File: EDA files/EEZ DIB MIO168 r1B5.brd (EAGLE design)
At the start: 146 x 95 mm, 301 parts, among them IC1 M24C32-WMN6P, IC10 DAC7760IPWPR, IC11 DAC7760IPWPR, IC12 OPA376AIDBVR, IC13 DAC7563TDGSR, IC14 OPA2196IDR, IC15 BTS3408G, IC16 BTS3408G, IC17 BTS3408G, IC18 BTS3408G, IC19 74HC126PW,118, IC2 Si8641BB-B-IS1, IC20 TL431B, IC21 DG468DV-T1-E3, IC22 DG468DV-T1-E3, IC23 DG468DV-T1-E3, IC24 DG468DV-T1-E3, IC25 DG468DV-T1-E3, IC26 DG468DV-T1-E3, IC27 DG468DV-T1-E3, IC28 DG468DV-T1-E3, IC29 DG468DV-T1-E3, IC3 Si8641BB-B-IS1, IC30 DG468DV-T1-E3, IC31 DG468DV-T1-E3, IC32 DG468DV-T1-E3, IC33 DG468DV-T1-E3, IC34 DG468DV-T1-E3, IC35 OPA376AIDBVR, IC36 ADS8674IDBT, IC4 L78L12, IC5 LM1117MP-5.0, IC6 LP2985-33DBVR, IC7 L79L12, IC8 STM32F446ZCT6, IC9 OPA2196IDR, J1 4907, J2 N.C., Q1 2N7002PS,115, Q10 BSS169, Q11 BSS169, Q12 BSS169, Q13 BSS169, Q2 2N7002PS,115, Q3 2N7002PS,115, Q4 2N7002PS,115, Q5 2N7002PS,115, Q6 BSS169, Q7 BSS169, Q8 BSS169, Q9 BSS169, X1 77317-104-28LF, X2 SSW-106-02-S-S, X3 691327310016, X4 691327310016, X5 1-2314878-0, X6 1-2314878-0, X7 1-2314878-0, Y1 25MHz

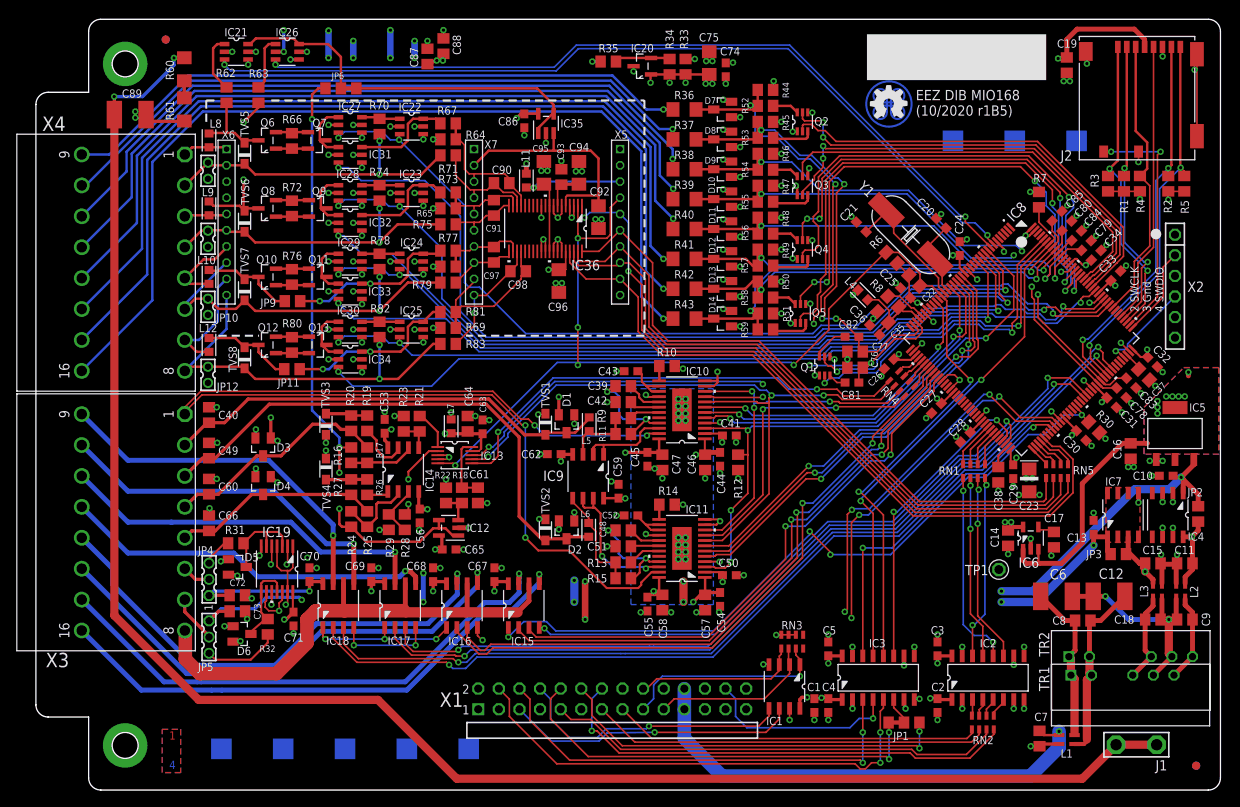
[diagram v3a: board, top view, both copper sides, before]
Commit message: ZD1, ZD2 added
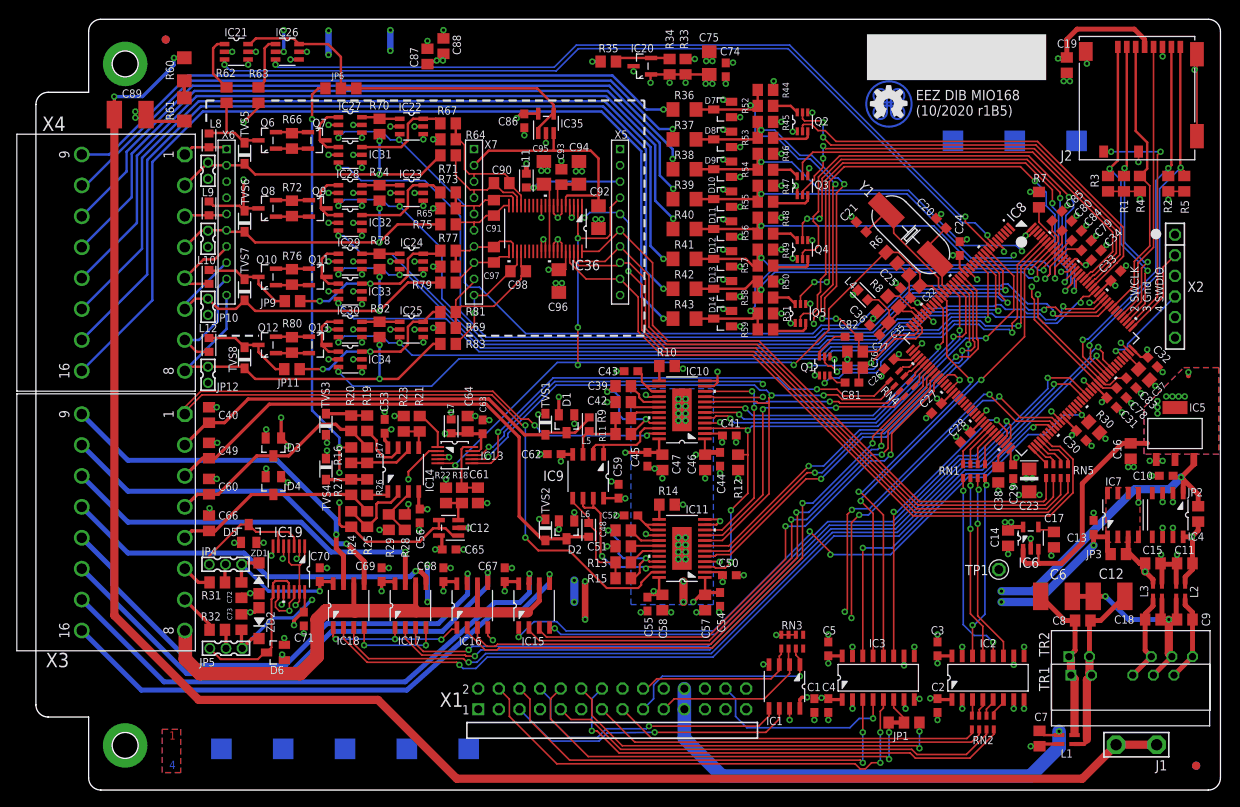
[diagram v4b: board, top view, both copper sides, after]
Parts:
- removed SH4: (no value), EEZ_Lib1:SHORT_NOHOLE
- added SH1: (no value), EEZ_Lib1:SHORT_NOHOLE
- added ZD1, ZD2: MMSZ4700T1G, EEZ_Lib1:SOD123
- moved SH2 26.8 mm to (18.2, 19.7), turned to 270 degrees
- moved R32 6.23 mm to (22.4, 19.7), turned to 180 degrees
- moved R31 5.34 mm to (22.4, 25.6), turned to 180 degrees
- moved D6 4.72 mm to (29.5, 17.0), turned to 90 degrees
- moved D5 4.36 mm to (26.2, 31.6), turned to 0 degrees
- moved JP4 2.74 mm to (23.4, 27.8), turned to 180 degrees
- moved JP5 2.52 mm to (23.4, 17.5), turned to 180 degrees
- moved IC19 1.46 mm to (31.2, 27.2)
- moved C73 1.43 mm to (25.3, 20.7), turned to 90 degrees
- moved C70 1.27 mm to (35.0, 26.5)
- moved C71 1.27 mm to (33.0, 21.1)
- moved IC16 1.27 mm to (53.8, 22.7)
- moved D3 1.27 mm to (29.3, 42.3)
- moved D4 1.27 mm to (29.3, 37.5)
- moved C67 1.27 mm to (57.8, 26.5)
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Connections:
- net +12V_ISO: now also ZD1.C
- net +3V3_ISO: now also D5.2, D6.2
- net +5V_ISO: no longer D5.2, D6.2
- net -12V_ISO: now also ZD2.C
- net -VSENSE: now also SH1.2; no longer SH2.2
- net GND: now also SH1.1, ZD1.A, ZD2.A; no longer SH4.1
- net N$1: now also SH2.2; no longer SH4.2
- net N$129: now also JP4.1; no longer R31.2
- net N$134: now also JP5.1; no longer R32.2
- net N$22: now also JP4.2; no longer JP4.1
- net N$25: now also R31.2; no longer JP4.2
- net N$39: now also R32.2; no longer JP5.2
- net N$40: now also JP5.2; no longer JP5.1
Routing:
- net +5V_ISO: track 282.3 -> 177.0 mm, vias 11 -> 9
- net N$134: track 11.0 -> 20.1 mm
- net N$40: track 9.45 -> 3.19 mm
- net -12V_ISO: track 260.8 -> 257.0 mm
- net N$129: track 12.3 -> 15.5 mm
- net +3V3_ISO: track 103.3 -> 106.4 mm, vias 35 -> 37
- net GND: track 228.3 -> 230.6 mm
- net +12V_ISO: track 262.5 -> 260.2 mm, vias 15 -> 14
- net N$1: track 73.5 -> 75.7 mm
- net OUT_EN: track 132.2 -> 130.1 mm
- net PWM#1: track 126.5 -> 124.4 mm
- net DOUT4: track 79.7 -> 78.0 mm
- net DOUT5: track 78.6 -> 76.9 mm
- net N$22: track 3.68 -> 2.25 mm
- net POUT5: track 61.6 -> 62.9 mm
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
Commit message: PWM outputs pin rearrangement
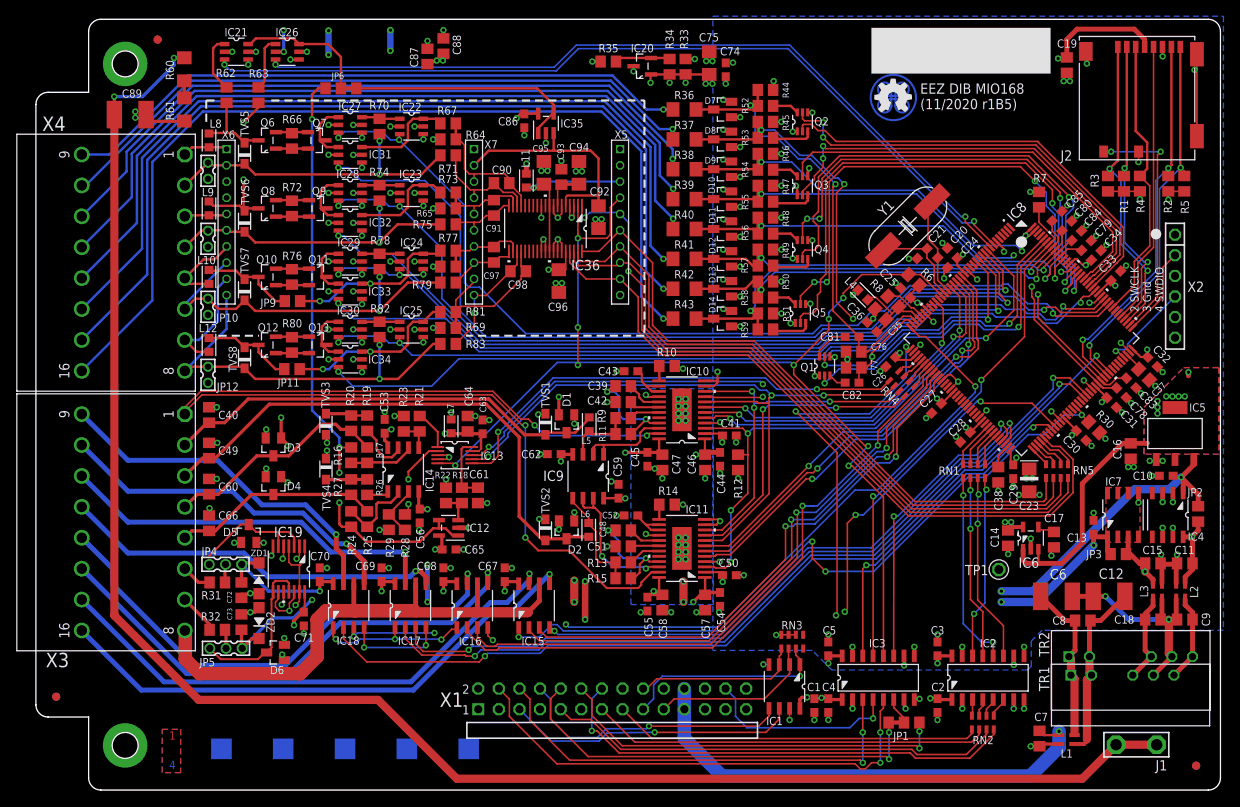
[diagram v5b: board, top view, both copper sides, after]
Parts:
- removed C22: N.C., rcl:C0805
- added FM3: FIDUCIAL_2, EEZ_Lib1:FIDUCIAL_DUAL
- R60, R61: value 560K -> 470K
- moved C21 8.18 mm to (109.2, 66.1), turned to 45 degrees
- moved C82 5.66 mm to (100.6, 50.2)
- moved C81 5.64 mm to (100.6, 55.9)
- moved R6 3.86 mm to (108.2, 62.9)
- moved C20 3.65 mm to (111.7, 66.2), turned to 225 degrees
- moved C77 1.98 mm to (100.8, 52.1)
- moved C24 1.97 mm to (113.0, 65.0), turned to 225 degrees
- moved C76 1.96 mm to (100.8, 54.0)
- moved Y1 1.13 mm to (107.5, 69.5), turned to 45 degrees
- moved FM1 1.00 mm to (15.0, 92.5)
- moved EEZ_SIGNATURE 0.97 mm to (105.7, 85.4)
- moved C36 0.49 mm to (103.0, 57.1)
- moved C35 0.46 mm to (104.1, 58.6)
- moved C26 0.34 mm to (105.4, 52.8)
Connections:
- net N$52 renamed +12V_CM
- net N$53 renamed GND_CM
- net !RESET: no longer C22.1
- net +3V3_ISO: no longer C22.2
- net DOUT1: now also IC8.36; no longer IC8.101
- net N$24: now also Q1.6; no longer Q1.3
- net N$76: now also Q1.3; no longer Q1.6
- net PWM#2: now also IC8.37; no longer IC8.82
- net SLOW_DIN#0: now also Q1.2; no longer Q1.5
- net SLOW_DIN#1: now also Q1.5; no longer Q1.2
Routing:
- net !RESET: track 160.6 -> 147.1 mm, vias 7 -> 9
- net DIN0: track 71.0 -> 58.0 mm, vias 5 -> 2
- net DOUT1: track 114.5 -> 102.2 mm, vias 2 -> 4
- net RCC_OSC_OUT: track 16.5 -> 11.8 mm
- net +3V3_ISO: track 106.4 -> 103.5 mm
- net RCC_OSC_IN: track 9.38 -> 12.1 mm
- net N$24: track 2.22 -> 4.63 mm
- net SLOW_DIN#1: track 41.1 -> 38.7 mm
- net N$76: track 4.53 -> 2.24 mm
- net DOUT4: track 78.0 -> 79.8 mm
- net !OUT_FAULT: track 116.9 -> 118.4 mm
- net SYNC: track 43.2 -> 41.7 mm
- net PWM#1: track 124.4 -> 123.0 mm
- net POUT0: track 45.0 -> 44.0 mm
- net DIN1: track 57.4 -> 58.5 mm
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- added copper zone on layer 16, net GND
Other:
- board text added: "EEZ DIB MIO168 (11/2020 r1B5)"
- board text added: "EEZ DIB MIO168 (11/2020 r1B5) Project source code: github.com/eez-open"
- board text removed: "EEZ DIB MIO168 (10/2020 r1B5)"
- board text removed: "EEZ DIB MIO168 (10/2020 r1B5) Project source code: github.com/eez-open"

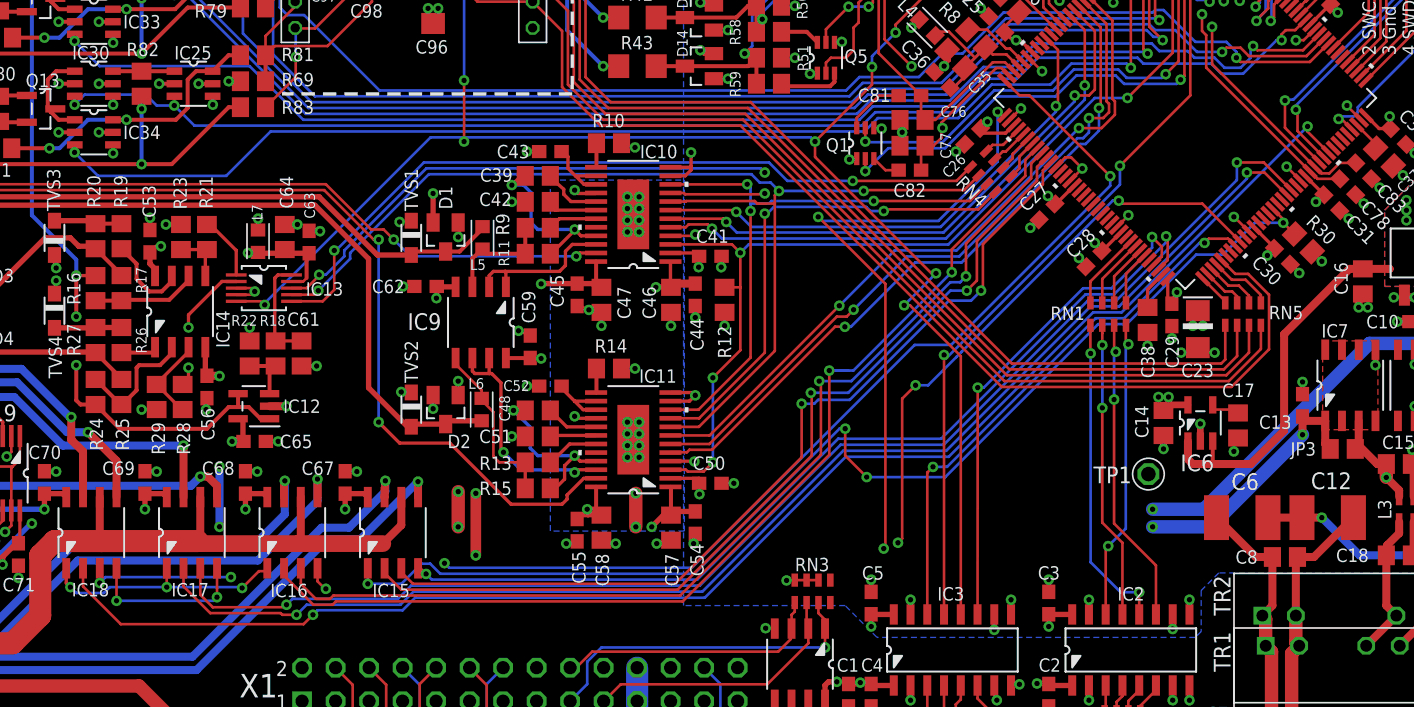
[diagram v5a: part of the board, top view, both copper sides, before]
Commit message: swap DOUT0 and DOUT1
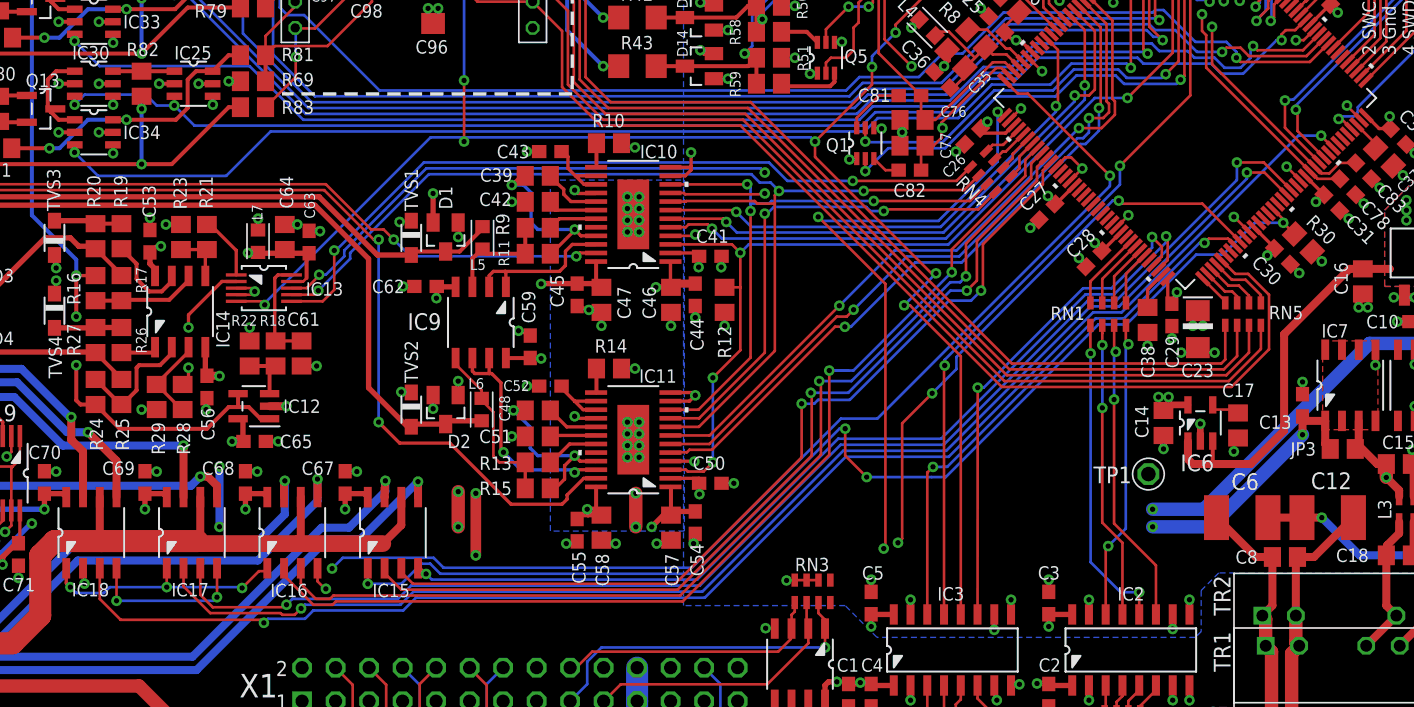
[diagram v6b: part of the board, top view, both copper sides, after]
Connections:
- net DOUT0: now also IC8.36; no longer IC8.100
- net DOUT1: now also IC8.101; no longer IC8.36
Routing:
- net DOUT0: track 114.0 -> 103.8 mm, vias 2 -> 3
- net DOUT1: track 102.2 -> 112.3 mm, vias 4 -> 2
- net PWM#1: track 123.0 -> 122.5 mm
